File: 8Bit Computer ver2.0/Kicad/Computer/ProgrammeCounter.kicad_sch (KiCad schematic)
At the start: 38 parts, among them IC155 SN74F521DWR, IC156 SN74F521DWR, IC157 SN74LVC1G14DBVR, IC158 SN74LVC1G14DBVR, IC159 SN74LVC1G14DBVR, IC160 SN74LVC1G08DBVR, IC161 SN74LVC1G32DBVR, IC162 SN74HCS4075DR, IC163 SN74LVC1G32DBVR, IC164 SN74LVC1G14DBVR, IC165 CY74FCT163CTSOC, IC166 CY74FCT163CTSOC, IC167 CY74FCT163CTSOC, IC168 CY74FCT163CTSOC, IC264 SN74AHC74DR, IC265 SN74LVC1G14DBVR

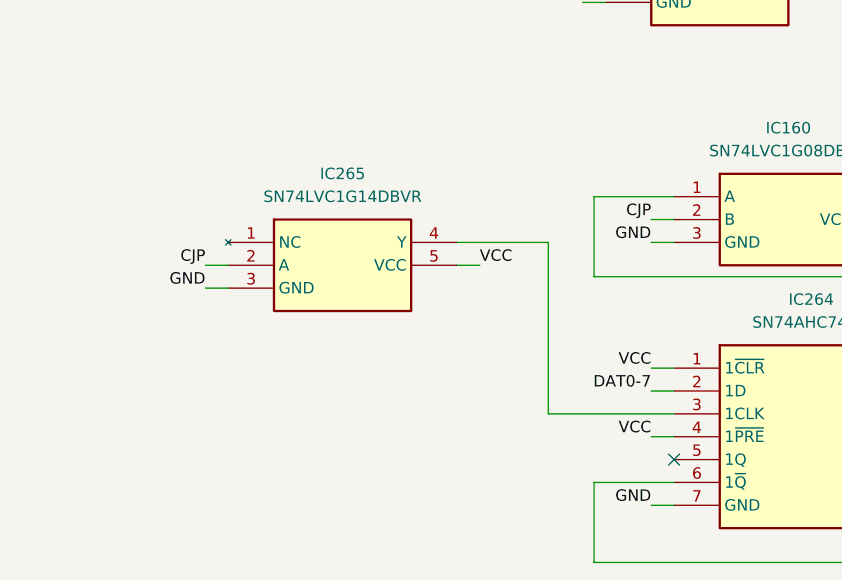
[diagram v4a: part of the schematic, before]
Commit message: Kicad Fixes only schematic
fixed important schematic errors
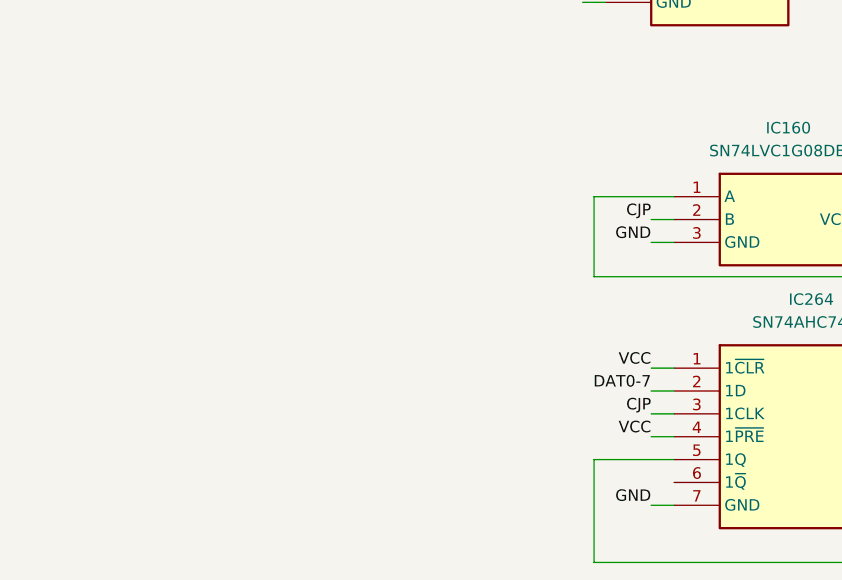
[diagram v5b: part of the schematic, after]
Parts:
- removed IC265: SN74LVC1G14DBVR, Samacsys:SOT95P280X145-5N, symbol Samacsys:SN74LVC1G14DBVR
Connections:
- net CJP: now also IC264.3 (1CLK)
- net at IC160.1 (A): now also IC264.5 (1Q); no longer IC264.6 (1~{Q})
- no-connect marks 4 -> 3
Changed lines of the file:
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@@
 	)
 	(no_connect
-		(at 213.36 243.84)
-	)
-	(no_connect
 		(at 243.84 248.92)
 	)
@@
 	(wire
 		(pts
-			(xy 213.36 246.38) (xy 204.47 246.38)
-		)
-		(stroke
-			(width 0)
-			(type default)
-		)
-	)
-	(wire
-		(pts
 			(xy 269.24 39.37) (xy 281.94 39.37)
 		)
@@
 	(wire
 		(pts
-			(xy 204.47 246.38) (xy 204.47 255.27)
-		)
-		(stroke
-			(width 0)
-			(type default)
-		)
-	)
-	(wire
-		(pts
-			(xy 189.23 222.25) (xy 191.77 222.25)
+			(xy 204.47 243.84) (xy 204.47 255.27)
 		)
 		(stroke
@@
 	(wire
 		(pts
+			(xy 213.36 243.84) (xy 204.47 243.84)
+		)
+		(stroke
+			(width 0)
+			(type default)
+		)
+	)
+	(wire
+		(pts
 			(xy 143.51 83.82) (xy 133.35 83.82)
 		)
@@
 	(wire
 		(pts
-			(xy 161.29 224.79) (xy 163.83 224.79)
-		)
-		(stroke
-			(width 0)
-			(type default)
-		)
-	)
-	(wire
-		(pts
 			(xy 133.35 76.2) (xy 135.89 76.2)
 		)
@@
 	(wire
 		(pts
-			(xy 161.29 222.25) (xy 163.83 222.25)
+			(xy 210.82 238.76) (xy 213.36 238.76)
 		)
 		(stroke
@@
 	(wire
 		(pts
-			(xy 199.39 238.76) (xy 213.36 238.76)
-		)
-		(stroke
-			(width 0)
-			(type default)
-		)
-	)
-	(wire
-		(pts
 			(xy 275.59 143.51) (xy 278.13 143.51)
 		)
@@
 		)
 	)
-	(wire
-		(pts
-			(xy 199.39 219.71) (xy 199.39 238.76)
-		)
-		(stroke
-			(width 0)
-			(type default)
-		)
-	)
 	(bus
 		(pts
@@
 		)
 	)
-	(wire
-		(pts
-			(xy 189.23 219.71) (xy 199.39 219.71)
-		)
-		(stroke
-			(width 0)
-			(type default)
-		)
-	)
 	(bus
 		(pts
@@
 		)
 	)
-	(label "GND"
-		(at 161.29 224.79 180)
-		(effects
-			(font
-				(size 1.27 1.27)
-			)
-			(justify right bottom)
-		)
-	)
 	(label "TC1"
 		(at 372.11 201.93 0)
@@
 	)
 	(label "CJP"
-		(at 161.29 222.25 180)
+		(at 210.82 238.76 180)
 		(effects
 			(font
@@
 		)
 	)
-	(label "VCC"
-		(at 191.77 222.25 0)
-		(effects
-			(font
-				(size 1.27 1.27)
-			)
-			(justify left bottom)
-		)
-	)
 	(label "ADR14"
 		(at 336.55 227.33 0)
@@
 					(unit 1)
 				)
-			)
-		)
-	)
-	(symbol
-		(lib_id "Samacsys:SN74LVC1G14DBVR")
-		(at 163.83 219.71 0)
-		(unit 1)
-		(exclude_from_sim no)
-		(in_bom yes)
-		(on_board yes)
-		(dnp no)
-		(fields_autoplaced yes)
-		(property "Reference" "IC265"
-			(at 176.53 212.09 0)
-			(effects
-				(font
-					(size 1.27 1.27)
-				)
-			)
-		)
-		(property "Value" "SN74LVC1G14DBVR"
-			(at 176.53 214.63 0)
-			(effects
-				(font
-					(size 1.27 1.27)
-				)
-			)
-		)
-		(property "Footprint" "Samacsys:SOT95P280X145-5N"
-			(at 185.42 314.63 0)
-			(effects
-				(font
-					(size 1.27 1.27)
-				)
-				(justify left top)
-				(hide yes)
-			)
-		)
-		(property "Datasheet" "https://datasheet.datasheetarchive.com/originals/distributors/Datasheets-DGA13/1136296.pdf"
-			(at 185.42 414.63 0)
-			(effects
-				(font
-					(size 1.27 1.27)
-				)
-				(justify left top)
-				(hide yes)
-			)
-		)
-		(property "Description" "TEXAS INSTRUMENTS - SN74LVC1G14DBVR - IC, SCHMITT TRIGGER INVERTER, SMD"
-			(at 163.83 219.71 0)
-			(effects
-				(font
-					(size 1.27 1.27)
-				)
-				(hide yes)
-			)
-		)
-		(property "Height" "1.45"
-			(at 185.42 614.63 0)
-			(effects
-				(font
-					(size 1.27 1.27)
-				)
-				(justify left top)
-				(hide yes)
-			)
-		)
-		(property "Mouser Part Number" "595-SN74LVC1G14DBVR"
-			(at 185.42 714.63 0)
-			(effects
-				(font
-					(size 1.27 1.27)
-				)
-				(justify left top)
-				(hide yes)
-			)
-		)
-		(property "Mouser Price/Stock" "https://www.mouser.co.uk/ProductDetail/Texas-Instruments/SN74LVC1G14DBVR?qs=dT9u2OTAaVWRIgCrQFnxuQ%3D%3D"
-			(at 185.42 814.63 0)
-			(effects
-				(font
-					(size 1.27 1.27)
-				)
-				(justify left top)
-				(hide yes)
-			)
-		)
-		(property "Manufacturer_Name" "Texas Instruments"
-			(at 185.42 914.63 0)
-			(effects
-				(font
-					(size 1.27 1.27)
-				)
-				(justify left top)
-				(hide yes)
-			)
-		)
-		(property "Manufacturer_Part_Number" "SN74LVC1G14DBVR"
-			(at 185.42 1014.63 0)
-			(effects
-				(font
-					(size 1.27 1.27)
-				)
-				(justify left top)
-				(hide yes)
-			)
-		)
-		(pin "1"
-		)
-		(pin "3"
-		)
-		(pin "2"
-		)
-		(pin "4"
-		)
-		(pin "5"
-		)
-		(instances
-			(project "Computer"
-				(path "/1196a00e-6878-4d6d-82b7-9e052dfe7c14/94b0c6d4-a0ed-4382-b2de-ee1cd48dbaa6"
-					(reference "IC265")
-					(unit 1)
-				)

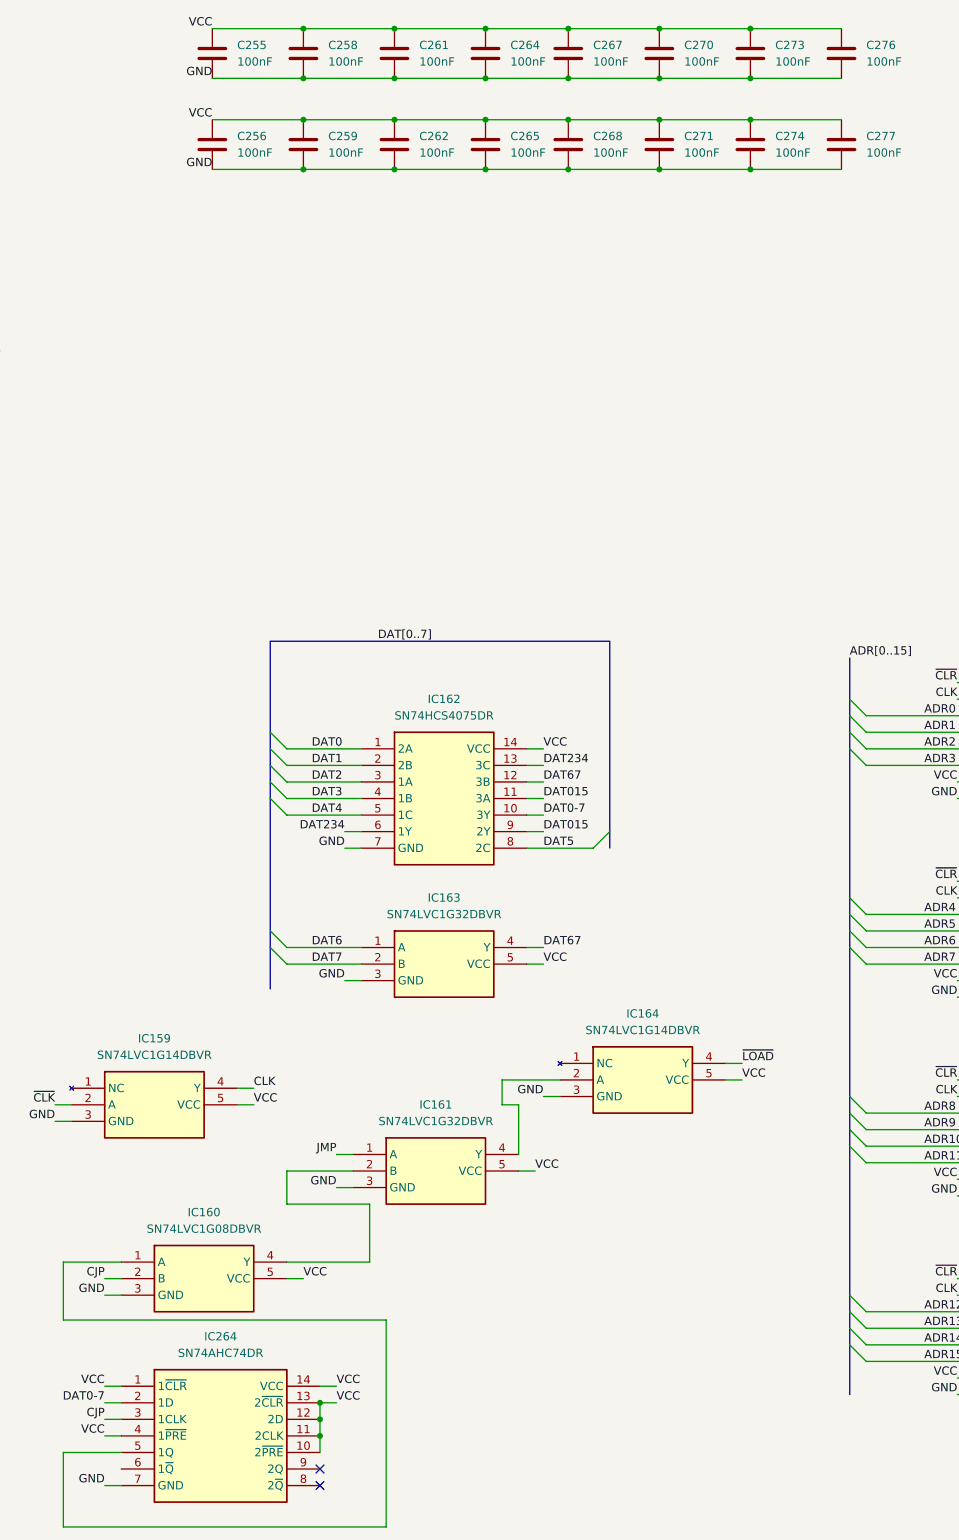
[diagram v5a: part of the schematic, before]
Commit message: Kicad, PCB Fix
fixed the errors on the PCB
added mounting holes
added GND panels on Top and Bot Layer
added 100uF
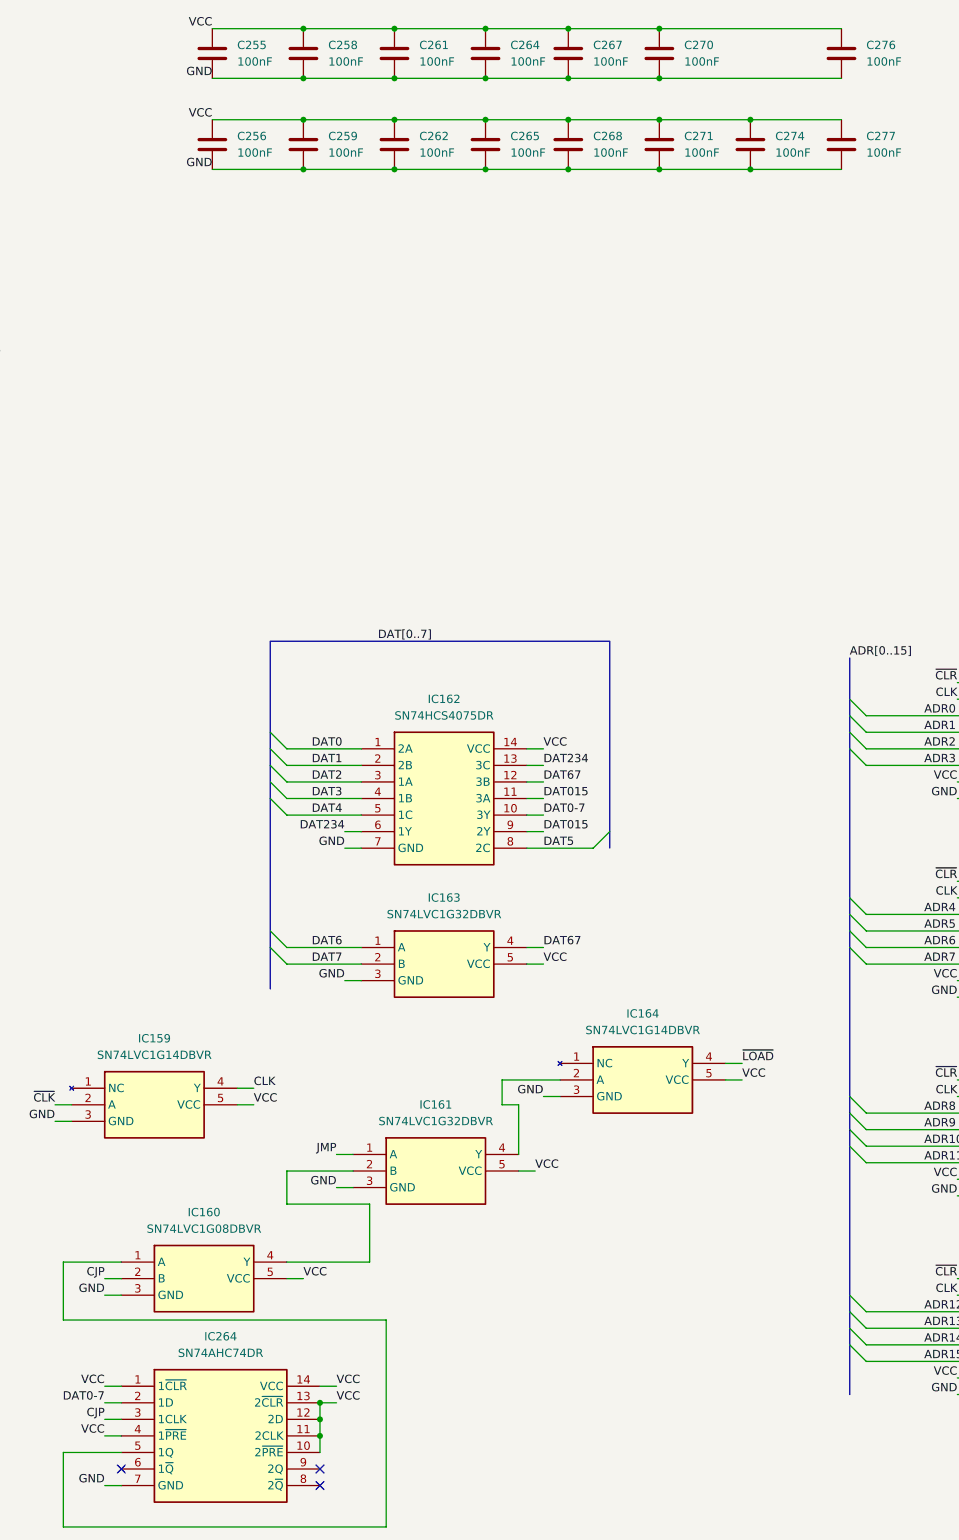
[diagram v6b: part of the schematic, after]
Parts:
- removed C273: 100nF, Capacitor_SMD:C_1206_3216Metric_Pad1.33x1.80mm_HandSolder, symbol Device:C
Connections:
- no-connect marks 3 -> 4
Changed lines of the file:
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@@
 	)
 	(junction
-		(at 309.88 25.4)
-		(diameter 0)
-		(color 0 0 0 0)
-	)
-	(junction
-		(at 309.88 33.02)
-		(diameter 0)
-		(color 0 0 0 0)
-	)
-	(junction
 		(at 269.24 33.02)
 		(diameter 0)
@@
 	)
 	(no_connect
+		(at 213.36 246.38)
+	)
+	(no_connect
 		(at 369.57 219.71)
 	)
@@
 	(wire
 		(pts
-			(xy 295.91 25.4) (xy 309.88 25.4)
+			(xy 295.91 25.4) (xy 323.85 25.4)
 		)
 		(stroke
@@
 	(wire
 		(pts
-			(xy 309.88 33.02) (xy 323.85 33.02)
-		)
-		(stroke
-			(width 0)
-			(type default)
-		)
-	)
-	(wire
-		(pts
 			(xy 100.33 91.44) (xy 102.87 91.44)
 		)
@@
 		)
 	)
-	(wire
-		(pts
-			(xy 309.88 25.4) (xy 323.85 25.4)
-		)
-		(stroke
-			(width 0)
-			(type default)
-		)
-	)
 	(bus
 		(pts
@@
 	(wire
 		(pts
-			(xy 295.91 33.02) (xy 309.88 33.02)
+			(xy 295.91 33.02) (xy 323.85 33.02)
 		)
 		(stroke
@@
 					(unit 1)
 				)
-			)
-		)
-	)
-	(symbol
-		(lib_id "Device:C")
-		(at 309.88 29.21 180)
-		(unit 1)
-		(exclude_from_sim no)
-		(in_bom yes)
-		(on_board yes)
-		(dnp no)
-		(fields_autoplaced yes)
-		(property "Reference" "C273"
-			(at 313.69 27.9399 0)
-			(effects
-				(font
-					(size 1.27 1.27)
-				)
-				(justify right)
-			)
-		)
-		(property "Value" "100nF"
-			(at 313.69 30.4799 0)
-			(effects
-				(font
-					(size 1.27 1.27)
-				)
-				(justify right)
-			)
-		)
-		(property "Footprint" "Capacitor_SMD:C_1206_3216Metric_Pad1.33x1.80mm_HandSolder"
-			(at 308.9148 25.4 0)
-			(effects
-				(font
-					(size 1.27 1.27)
-				)
-				(hide yes)
-			)
-		)
-		(property "Datasheet" "~"
-			(at 309.88 29.21 0)
-			(effects
-				(font
-					(size 1.27 1.27)
-				)
-				(hide yes)
-			)
-		)
-		(property "Description" "Unpolarized capacitor"
-			(at 309.88 29.21 0)
-			(effects
-				(font
-					(size 1.27 1.27)
-				)
-				(hide yes)
-			)
-		)
-		(pin "1"
-		)
-		(pin "2"
-		)
-		(instances
-			(project "Computer"
-				(path "/1196a00e-6878-4d6d-82b7-9e052dfe7c14/94b0c6d4-a0ed-4382-b2de-ee1cd48dbaa6"
-					(reference "C273")
-					(unit 1)
-				)

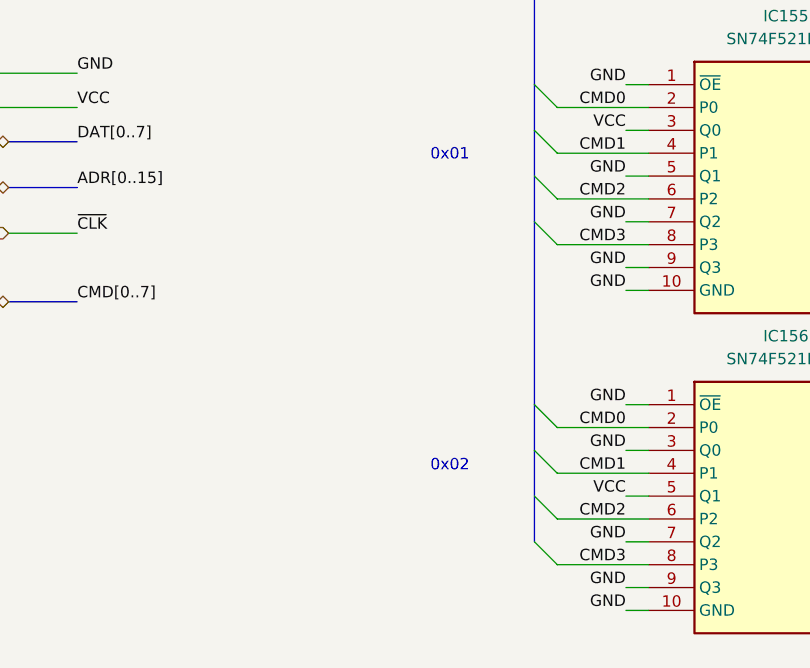
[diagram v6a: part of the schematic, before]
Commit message: Kicad
fixed some design errors(dat dis DistShiftreg, wrong cmd pins)
added description to every CMD for better debug, use CTRL+f and use option "Whole words only" to search e.g. inc
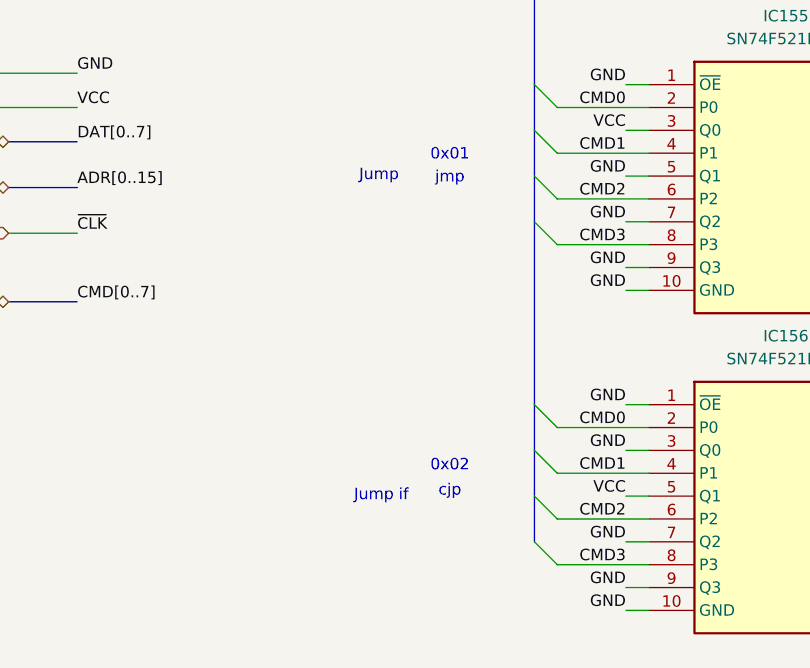
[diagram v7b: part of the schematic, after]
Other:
- note added: "Jump"
- note added: "Jump if"
- note added: "cjp"
- note added: "jmp"
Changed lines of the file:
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@@
+		)
+	)
+	(text "Jump"
+		(exclude_from_sim no)
+		(at 72.898 86.36 0)
+		(effects
+			(font
+				(size 1.27 1.27)
+			)
 		)
 	)
@@
 		(exclude_from_sim no)
 		(at 80.772 85.09 0)
+		(effects
+			(font
+				(size 1.27 1.27)
+			)
+		)
+	)
+	(text "jmp"
+		(exclude_from_sim no)
+		(at 80.772 86.614 0)
 		(effects
 			(font
@@
 			)
 		)
+	)
+	(text "cjp"
+		(exclude_from_sim no)
+		(at 80.772 121.412 0)
+		(effects
+			(font
+				(size 1.27 1.27)
+			)
+		)
+	)
+	(text "Jump if"
+		(exclude_from_sim no)
+		(at 73.152 121.92 0)
+		(effects
+			(font
+				(size 1.27 1.27)
+			)
+		)
